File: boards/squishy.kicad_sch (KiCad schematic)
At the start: 45 parts, among them J1 USB_B_Micro, J2 Conn_02x26_Top_Bottom, J3 Conn_02x05_Odd_Even, Q1 Q_PMOS_DGS, U1 W25N01GVZEIG, U2 ICE40HX8K-BG121, U3 USB3318, X1 48MHz, X2 16MHz

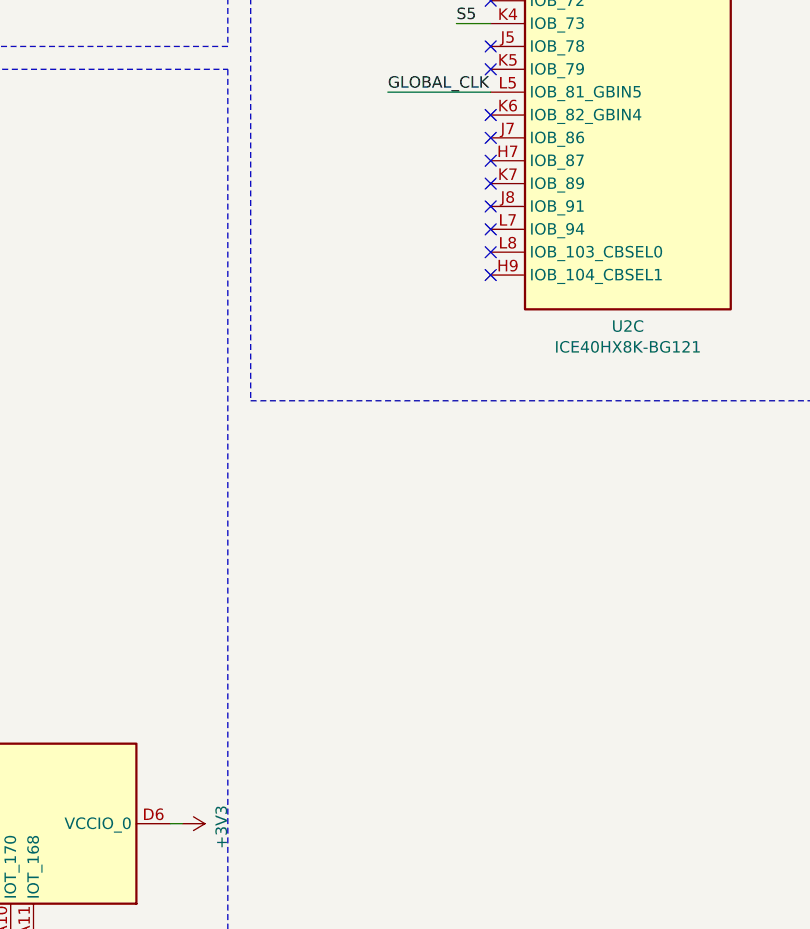
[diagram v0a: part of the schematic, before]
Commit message: Added a UART for debugging
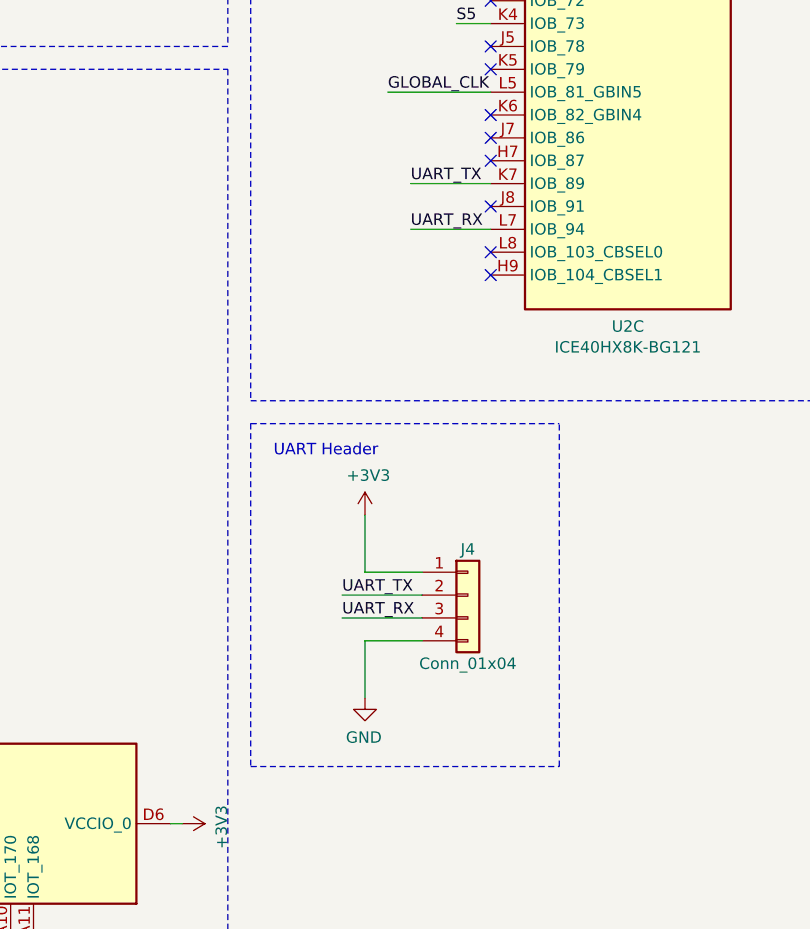
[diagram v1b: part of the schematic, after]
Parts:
- added J4: Conn_01x04, Connector_PinHeader_1.27mm:PinHeader_1x04_P1.27mm_Vertical, symbol Connector_Generic:Conn_01x04
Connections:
- net +3V3: now also J4.1 (Pin_1)
- net GND: now also J4.4 (Pin_4)
- net UART_TX: now reaches U2.K7 (IOB_89)
- net UART_TX: now also J4.2 (Pin_2)
- net UART_RX: now reaches U2.L7 (IOB_94)
- net UART_RX: now also J4.3 (Pin_3)
- no-connect marks 32 -> 30
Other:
- note added: "UART Header"
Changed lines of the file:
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@@
   (no_connect (at 246.38 135.89))
   (no_connect (at 246.38 138.43))
-  (no_connect (at 246.38 140.97))
   (no_connect (at 246.38 143.51))
-  (no_connect (at 246.38 146.05))
   (no_connect (at 246.38 148.59))
   (no_connect (at 246.38 151.13))
@@
     (stroke (width 0) (type solid) (color 0 0 0 0))
   )
+  (wire (pts (xy 232.41 177.8) (xy 232.41 184.15))
+    (stroke (width 0) (type solid) (color 0 0 0 0))
+  )
+  (wire (pts (xy 232.41 184.15) (xy 238.76 184.15))
+    (stroke (width 0) (type solid) (color 0 0 0 0))
+  )
+  (wire (pts (xy 232.41 191.77) (xy 232.41 198.12))
+    (stroke (width 0) (type solid) (color 0 0 0 0))
+  )
   (wire (pts (xy 233.68 41.91) (xy 251.46 41.91))
     (stroke (width 0) (type solid) (color 0 0 0 0))
   )
+  (wire (pts (xy 238.76 186.69) (xy 229.87 186.69))
+    (stroke (width 0) (type solid) (color 0 0 0 0))
+  )
+  (wire (pts (xy 238.76 189.23) (xy 229.87 189.23))
+    (stroke (width 0) (type solid) (color 0 0 0 0))
+  )
+  (wire (pts (xy 238.76 191.77) (xy 232.41 191.77))
+    (stroke (width 0) (type solid) (color 0 0 0 0))
+  )
   (wire (pts (xy 246.38 97.79) (xy 231.14 97.79))
     (stroke (width 0) (type solid) (color 0 0 0 0))
@@
     (stroke (width 0) (type solid) (color 0 0 0 0))
   )
+  (wire (pts (xy 246.38 140.97) (xy 237.49 140.97))
+    (stroke (width 0) (type solid) (color 0 0 0 0))
+  )
+  (wire (pts (xy 246.38 146.05) (xy 237.49 146.05))
+    (stroke (width 0) (type solid) (color 0 0 0 0))
+  )
   (wire (pts (xy 261.62 86.36) (xy 261.62 90.17))
     (stroke (width 0) (type solid) (color 0 0 0 0))
@@
     (stroke (width 0) (type dash) (color 0 0 0 0))
   )
+  (polyline (pts (xy 219.71 167.64) (xy 219.71 205.74))
+    (stroke (width 0) (type dash) (color 0 0 0 0))
+  )
+  (polyline (pts (xy 219.71 167.64) (xy 254 167.64))
+    (stroke (width 0) (type dash) (color 0 0 0 0))
+  )
+  (polyline (pts (xy 219.71 205.74) (xy 254 205.74))
+    (stroke (width 0) (type dash) (color 0 0 0 0))
+  )
+  (polyline (pts (xy 254 205.74) (xy 254 167.64))
+    (stroke (width 0) (type dash) (color 0 0 0 0))
+  )
   (polyline (pts (xy 255.27 69.85) (xy 255.27 13.97))
     (stroke (width 0) (type dash) (color 0 0 0 0))
@@
     (effects (font (size 1.27 1.27)) (justify left bottom))
   )
+  (text "UART Header" (at 222.25 171.45 0)
+    (effects (font (size 1.27 1.27)) (justify left bottom))
+  )
   (text "Status LEDs" (at 260.35 17.78 0)
     (effects (font (size 1.27 1.27)) (justify left bottom))
@@
     (effects (font (size 1.27 1.27)) (justify right bottom))
   )
+  (label "UART_TX" (at 229.87 186.69 0)
+    (effects (font (size 1.27 1.27)) (justify left bottom))
+  )
+  (label "UART_RX" (at 229.87 189.23 0)
+    (effects (font (size 1.27 1.27)) (justify left bottom))
+  )
   (label "~{FPGA_RESET}" (at 232.41 97.79 0)
     (effects (font (size 1.27 1.27)) (justify left bottom))
@@
     (effects (font (size 1.27 1.27)) (justify left bottom))
   )
+  (label "UART_TX" (at 237.49 140.97 0)
+    (effects (font (size 1.27 1.27)) (justify left bottom))
+  )
+  (label "UART_RX" (at 237.49 146.05 0)
+    (effects (font (size 1.27 1.27)) (justify left bottom))
+  )
   (label "S1" (at 242.57 105.41 0)
     (effects (font (size 1.27 1.27)) (justify left bottom))
@@
     (pin "1")
   )
+  (symbol (lib_id "power:+3V3") (at 232.41 177.8 0) (unit 1)
+    (in_bom yes) (on_board yes)
+    (property "Reference" "#PWR0238" (id 0) (at 232.41 181.61 0)
+      (effects (font (size 1.27 1.27)) hide)
+    )
+    (property "Value" "+3V3" (id 1) (at 232.791 173.4058 0))
+    (property "Footprint" "" (id 2) (at 232.41 177.8 0)
+      (effects (font (size 1.27 1.27)) hide)
+    )
+    (property "Datasheet" "" (id 3) (at 232.41 177.8 0)
+      (effects (font (size 1.27 1.27)) hide)
+    )
+    (pin "1")
+  )
   (symbol (lib_id "power:+3V3") (at 261.62 86.36 0) (unit 1)
     (in_bom yes) (on_board yes)
@@
     (pin "1")
   )
+  (symbol (lib_id "power:GND") (at 232.41 198.12 0) (mirror y) (unit 1)
+    (in_bom yes) (on_board yes)
+    (property "Reference" "#PWR0237" (id 0) (at 232.41 204.47 0)
+      (effects (font (size 1.27 1.27)) hide)
+    )
+    (property "Value" "GND" (id 1) (at 232.283 202.5142 0))
+    (property "Footprint" "" (id 2) (at 232.41 198.12 0)
+      (effects (font (size 1.27 1.27)) hide)
+    )
+    (property "Datasheet" "" (id 3) (at 232.41 198.12 0)
+      (effects (font (size 1.27 1.27)) hide)
+    )
+    (pin "1")
+  )
   (symbol (lib_id "power:GND") (at 295.91 50.8 0) (mirror y) (unit 1)
     (in_bom yes) (on_board yes)
@@
     (pin "2")
   )
+  (symbol (lib_id "Connector_Generic:Conn_01x04") (at 243.84 186.69 0) (unit 1)
+    (in_bom yes) (on_board yes)
+    (property "Reference" "J4" (id 0) (at 243.84 181.61 0))
+    (property "Value" "Conn_01x04" (id 1) (at 243.84 194.31 0))
+    (property "Footprint" "Connector_PinHeader_1.27mm:PinHeader_1x04_P1.27mm_Vertical" (id 2) (at 243.84 186.69 0)
+      (effects (font (size 1.27 1.27)) hide)
+    )
+    (property "Datasheet" "~" (id 3) (at 243.84 186.69 0)
+      (effects (font (size 1.27 1.27)) hide)
+    )
+    (pin "1")
+    (pin "2")
+    (pin "3")
+    (pin "4")
+  )
   (symbol (lib_id "Device:Q_PMOS_GSD") (at 34.29 255.27 270) (mirror x) (unit 1)
     (in_bom yes) (on_board yes)
@@
       (reference "#PWR0236") (unit 1) (value "GND") (footprint "")
     )
+    (path "/bb2bcdc6-906b-4745-a8f8-4756f2dee710"
+      (reference "#PWR0237") (unit 1) (value "GND") (footprint "")
+    )
+    (path "/ad6201a3-1522-453e-a3b3-2bfce175f37f"
+      (reference "#PWR0238") (unit 1) (value "+3V3") (footprint "")
+    )
     (path "/00000000-0000-0000-0000-00005f0d7af1"
       (reference "C1") (unit 1) (value "0.1uF") (footprint "Capacitor_SMD:C_0603_1608Metric")
@@
       (reference "J3") (unit 1) (value "Conn_02x05_Odd_Even") (footprint "lethalbit-connectors:FTSH-105-01-L-DV-K-TR")
     )
+    (path "/fdd49bc0-b607-47bd-ada3-ca103a94c465"
+      (reference "J4") (unit 1) (value "Conn_01x04") (footprint "Connector_PinHeader_1.27mm:PinHeader_1x04_P1.27mm_Vertical")
+    )
     (path "/ebece55b-2991-4037-9810-87879324b66b"

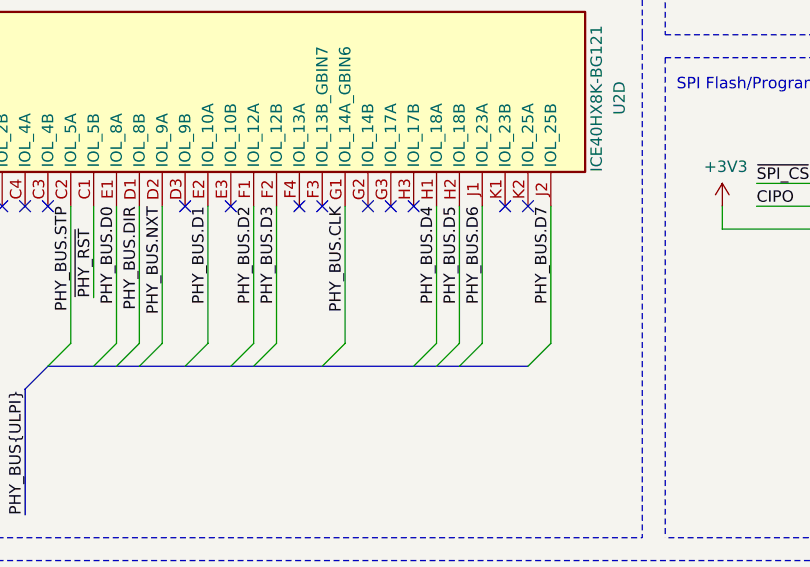
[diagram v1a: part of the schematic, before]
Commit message: hardware: shuffled some pins around to make the ulpi traces nicer
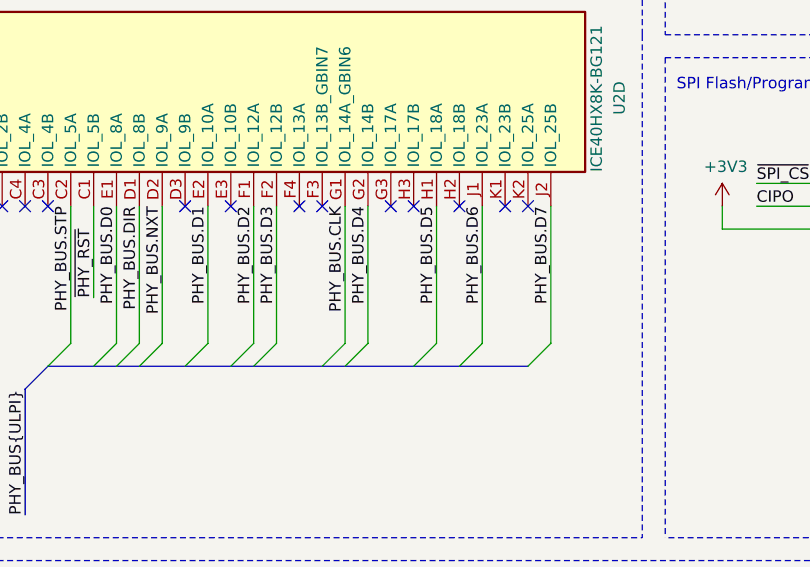
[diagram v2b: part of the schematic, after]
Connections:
- net PHY_BUS.D4: now also U2.G2 (IOL_14B); no longer U2.H1 (IOL_18A)
- net PHY_BUS.D5: now also U2.H1 (IOL_18A); no longer U2.H2 (IOL_18B)
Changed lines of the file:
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@@
     (company "Aki")
   )
+  (bus_alias "SCSI-SE" (members "DB[0..7]" "DBP" "IO" "REQ" "CD" "SEL" "MSG" "RST" "ACK" "BSY" "ATN"))
+  (bus_alias "SCSI-DIFF" (members "DBP+" "DBP-" "ATN+" "ATN-" "BSY+" "BSY-" "ACK+" "ACK-" "RST+" "RST-" "MSG+" "MSG-" "SEL+" "SEL-" "CD+" "CD-" "REQ+" "REQ-" "IO+" "IO-" "DB0+" "DB0-" "DB1+" "DB1-" "DB2+" "DB2-" "DB3+" "DB3-" "DB4+" "DB4-" "DB5+" "DB5-" "DB6+" "DB6-" "DB7+" "DB7-"))
   (bus_alias "ULPI" (members "D[0..7]" "CLK" "STP" "DIR" "NXT"))
-  (bus_alias "SCSI-DIFF" (members "DBP+" "DBP-" "ATN+" "ATN-" "BSY+" "BSY-" "ACK+" "ACK-" "RST+" "RST-" "MSG+" "MSG-" "SEL+" "SEL-" "CD+" "CD-" "REQ+" "REQ-" "IO+" "IO-" "DB0+" "DB0-" "DB1+" "DB1-" "DB2+" "DB2-" "DB3+" "DB3-" "DB4+" "DB4-" "DB5+" "DB5-" "DB6+" "DB6-" "DB7+" "DB7-"))
-  (bus_alias "SCSI-SE" (members "DB[0..7]" "DBP" "IO" "REQ" "CD" "SEL" "MSG" "RST" "ACK" "BSY" "ATN"))
   (junction (at 19.05 55.88) (diameter 1.016) (color 0 0 0 0))
   (junction (at 27.94 49.53) (diameter 1.016) (color 0 0 0 0))
@@
   (no_connect (at 116.84 88.9))
   (no_connect (at 119.38 88.9))
-  (no_connect (at 124.46 88.9))
   (no_connect (at 127 88.9))
   (no_connect (at 129.54 88.9))
+  (no_connect (at 134.62 88.9))
   (no_connect (at 139.7 88.9))
   (no_connect (at 142.24 88.9))
@@
     (stroke (width 0.1524) (type solid) (color 0 0 0 0))
   )
+  (bus_entry (at 121.92 106.68) (size 2.54 -2.54)
+    (stroke (width 0.1524) (type solid) (color 0 0 0 0))
+  )
   (bus_entry (at 121.92 135.89) (size 2.54 2.54)
     (stroke (width 0.1524) (type solid) (color 0 0 0 0))
@@
     (stroke (width 0.1524) (type solid) (color 0 0 0 0))
   )
-  (bus_entry (at 132.08 106.68) (size 2.54 -2.54)
-    (stroke (width 0.1524) (type solid) (color 0 0 0 0))
-  )
   (bus_entry (at 134.62 106.68) (size 2.54 -2.54)
     (stroke (width 0.1524) (type solid) (color 0 0 0 0))
@@
     (stroke (width 0) (type solid) (color 0 0 0 0))
   )
+  (wire (pts (xy 124.46 104.14) (xy 124.46 88.9))
+    (stroke (width 0) (type solid) (color 0 0 0 0))
+  )
   (wire (pts (xy 124.46 138.43) (xy 137.16 138.43))
     (stroke (width 0) (type solid) (color 0 0 0 0))
@@
     (stroke (width 0) (type solid) (color 0 0 0 0))
   )
-  (wire (pts (xy 134.62 104.14) (xy 134.62 88.9))
-    (stroke (width 0) (type solid) (color 0 0 0 0))
-  )
   (wire (pts (xy 137.16 104.14) (xy 137.16 88.9))
     (stroke (width 0) (type solid) (color 0 0 0 0))
@@
     (effects (font (size 1.27 1.27)) (justify right bottom))
   )
-  (label "PHY_BUS.D4" (at 132.08 88.9 270)
-    (effects (font (size 1.27 1.27)) (justify right bottom))
-  )
-  (label "PHY_BUS.D5" (at 134.62 88.9 270)
-    (effects (font (size 1.27 1.27)) (justify right bottom))
-  )
+  (label "PHY_BUS.D4" (at 124.46 88.9 270)
+    (effects (font (size 1.27 1.27)) (justify right bottom))
+  )
+  (label "PHY_BUS.D5" (at 132.08 88.9 270)
+    (effects (font (size 1.27 1.27)) (justify right bottom))
+  )

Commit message: hardware: something updated but i don't know what it was
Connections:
- net PHY_BUS.D6: now also U2.H2 (IOL_18B); no longer U2.J1 (IOL_23A)
- net PHY_BUS.D7: now also U2.J1 (IOL_23A); no longer U2.J2 (IOL_25B)
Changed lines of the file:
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@@
   (no_connect (at 127 88.9))
   (no_connect (at 129.54 88.9))
-  (no_connect (at 134.62 88.9))
   (no_connect (at 139.7 88.9))
   (no_connect (at 142.24 88.9))
+  (no_connect (at 149.86 92.71))
   (no_connect (at 152.4 224.79))
   (no_connect (at 177.8 224.79))
@@
     (stroke (width 0.1524) (type solid) (color 0 0 0 0))
   )
+  (bus_entry (at 132.08 106.68) (size 2.54 -2.54)
+    (stroke (width 0.1524) (type solid) (color 0 0 0 0))
+  )
   (bus_entry (at 134.62 106.68) (size 2.54 -2.54)
     (stroke (width 0.1524) (type solid) (color 0 0 0 0))
   )
-  (bus_entry (at 142.24 106.68) (size 2.54 -2.54)
-    (stroke (width 0.1524) (type solid) (color 0 0 0 0))
-  )
   (wire (pts (xy 16.51 152.4) (xy 29.21 152.4))
     (stroke (width 0) (type solid) (color 0 0 0 0))
@@
     (stroke (width 0) (type solid) (color 0 0 0 0))
   )
+  (wire (pts (xy 134.62 104.14) (xy 134.62 88.9))
+    (stroke (width 0) (type solid) (color 0 0 0 0))
+  )
   (wire (pts (xy 137.16 104.14) (xy 137.16 88.9))
     (stroke (width 0) (type solid) (color 0 0 0 0))
@@
     (stroke (width 0) (type solid) (color 0 0 0 0))
   )
-  (wire (pts (xy 144.78 104.14) (xy 144.78 88.9))
-    (stroke (width 0) (type solid) (color 0 0 0 0))
-  )
   (wire (pts (xy 144.78 224.79) (xy 144.78 237.49))
     (stroke (width 0) (type solid) (color 0 0 0 0))
@@
     (effects (font (size 1.27 1.27)) (justify right bottom))
   )
-  (label "PHY_BUS.D6" (at 137.16 88.9 270)
+  (label "PHY_BUS.D6" (at 134.62 88.9 270)
+    (effects (font (size 1.27 1.27)) (justify right bottom))
+  )
+  (label "PHY_BUS.D7" (at 137.16 88.9 270)
     (effects (font (size 1.27 1.27)) (justify right bottom))
   )
@@
     (effects (font (size 1.27 1.27)) (justify left bottom))
   )
-  (label "PHY_BUS.D7" (at 144.78 88.9 270)
-    (effects (font (size 1.27 1.27)) (justify right bottom))
-  )
   (label "SCSI-RX.IO" (at 144.78 237.49 90)

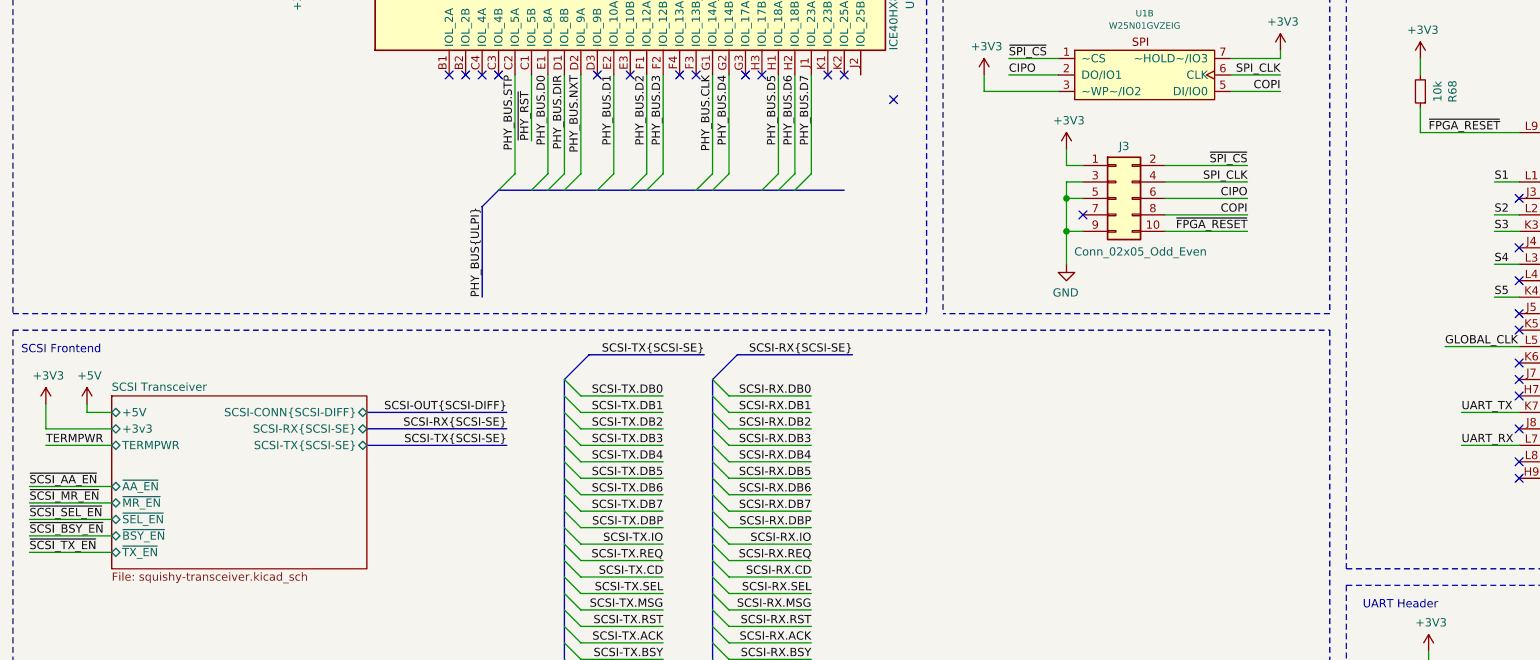
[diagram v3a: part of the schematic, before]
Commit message: hardware: added some additional test points
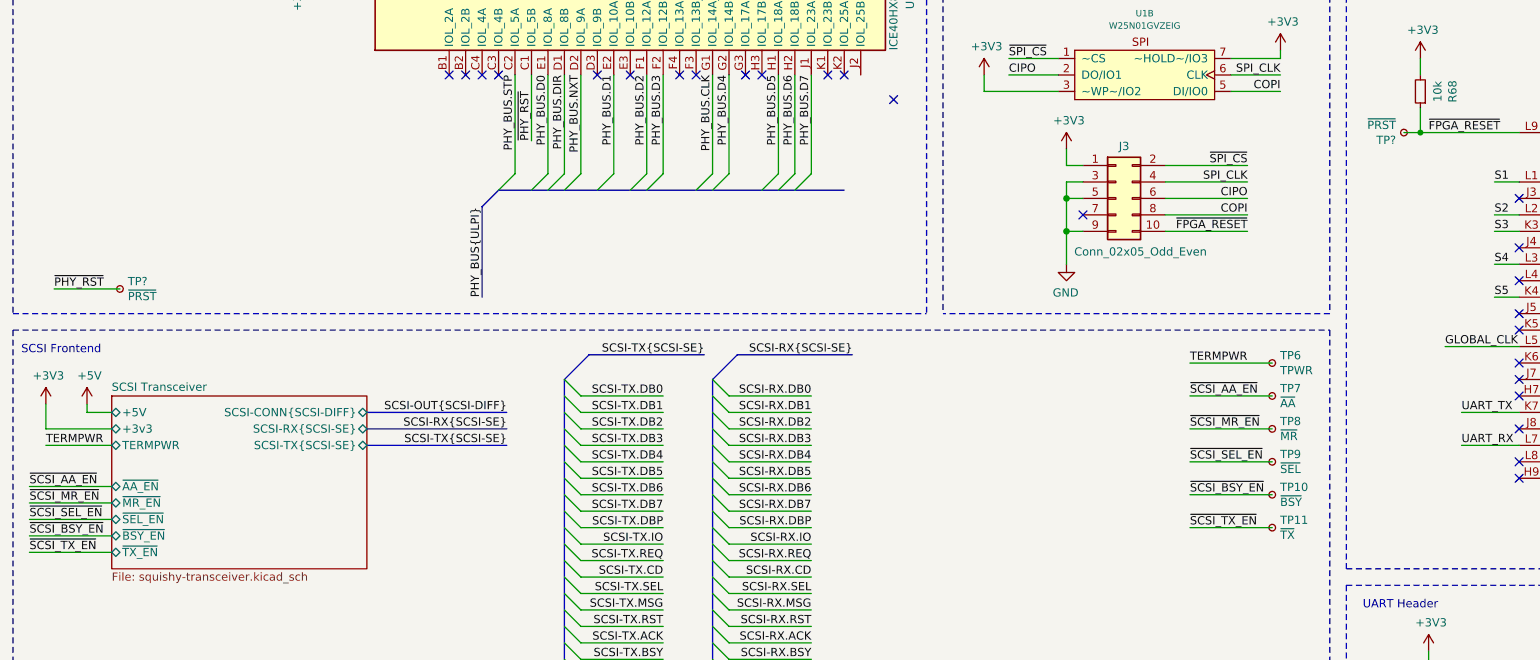
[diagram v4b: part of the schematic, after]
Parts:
- added TP10: ~{BSY}, TestPoint:TestPoint_Pad_D1.0mm, symbol Connector:TestPoint_Small
- added TP11: ~{TX}, TestPoint:TestPoint_Pad_D1.0mm, symbol Connector:TestPoint_Small
- added TP6: TPWR, TestPoint:TestPoint_Pad_D1.0mm, symbol Connector:TestPoint_Small
- added TP7: ~{AA}, TestPoint:TestPoint_Pad_D1.0mm, symbol Connector:TestPoint_Small
- added TP8: ~{MR}, TestPoint:TestPoint_Pad_D1.0mm, symbol Connector:TestPoint_Small
- added TP9: ~{SEL}, TestPoint:TestPoint_Pad_D1.0mm, symbol Connector:TestPoint_Small
- added TP? (x2): ~{PRST}, TestPoint:TestPoint_Pad_D1.0mm, symbol Connector:TestPoint_Small
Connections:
- net TERMPWR: now also TP6.1
- net ~{FPGA_RESET}: now also TP?.1
- net ~{PHY_RST}: now also TP?.1
- net ~{SCSI_AA_EN}: now also TP7.1
- net ~{SCSI_BSY_EN}: now also TP10.1
- net ~{SCSI_MR_EN}: now also TP8.1
- net ~{SCSI_SEL_EN}: now also TP9.1
- net ~{SCSI_TX_EN}: now also TP11.1
